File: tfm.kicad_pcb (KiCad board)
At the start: 2 copper layers, 100 x 90 mm, 93 parts, among them J1 Screw_Terminal_01x04, J2 Screw_Terminal_01x04, J3 Conn_01x03, J4 Conn_01x03, J5 Conn_01x03, J6 Conn_02x04_Counter_Clockwise, U1 LPS25HB, U10 MCP6004, U11 MCP6004, U12 ZMPT101B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

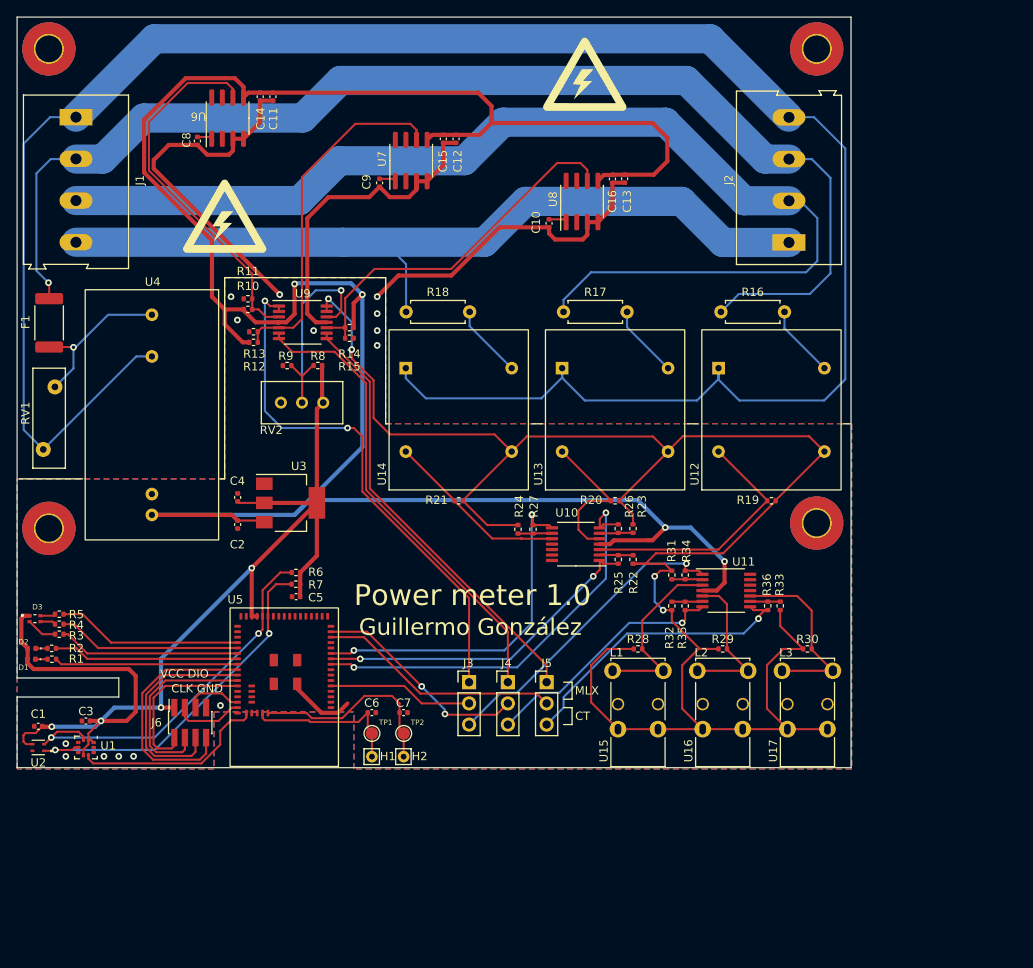
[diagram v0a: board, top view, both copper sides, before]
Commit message: Edge cuts with curves
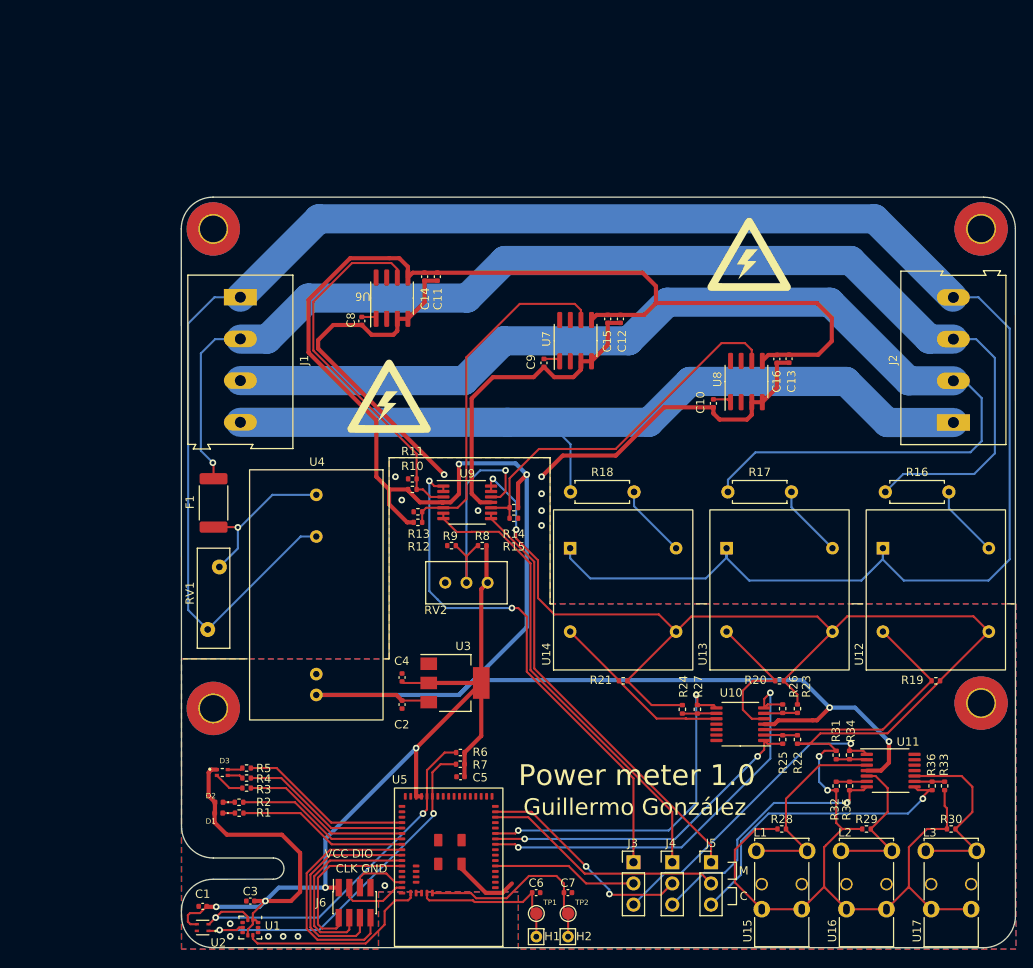
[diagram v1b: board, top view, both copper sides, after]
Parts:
- moved R16 29.2 mm to (182.9, 82.3)
- moved F1 29.2 mm to (102.3, 83.7)
- moved R8 29.2 mm to (134.5, 88.8)
- moved R9 29.2 mm to (130.8, 88.8)
- moved C1 29.2 mm to (101.0, 132.0)
- moved C10 29.2 mm to (162.2, 71.7)
- moved C11 29.2 mm to (129.1, 56.5)
- moved C12 29.2 mm to (151.1, 61.6)
- moved C14 29.2 mm to (127.6, 56.5)
- moved C15 29.2 mm to (149.6, 61.6)
- moved C16 29.2 mm to (169.8, 66.4)
- moved C2 29.2 mm to (124.9, 107.8)
- moved C3 29.2 mm to (106.7, 131.4)
- moved C4 29.2 mm to (124.9, 104.6)
- moved C8 29.2 mm to (120.1, 61.8)
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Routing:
- net /power_sensors/2V5: track 226.8 -> 221.7 mm
- net Net-(R28-Pad2): track 22.2 -> 24.8 mm
- net /power_sensors/ct3_out: track 35.0 -> 36.6 mm
- net /LED2: track 22.3 -> 20.9 mm
- net /LEDB: track 22.3 -> 20.8 mm
- net /LED1: track 22.0 -> 20.6 mm
- net /LEDG: track 22.0 -> 20.6 mm
- net /LEDR: track 21.8 -> 20.4 mm
- net /power_sensors/ct2_out: track 29.9 -> 31.3 mm
- net +3V3: track 135.1 -> 134.3 mm
- net Net-(R30-Pad2): track 22.5 -> 23.1 mm
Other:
- outline, holes or cut-outs redrawn
- board text added: "C"
- board text added: "M"
- board text removed: "CT"
- board text removed: "MLX"

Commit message: Fix jack orientation and add 3d model
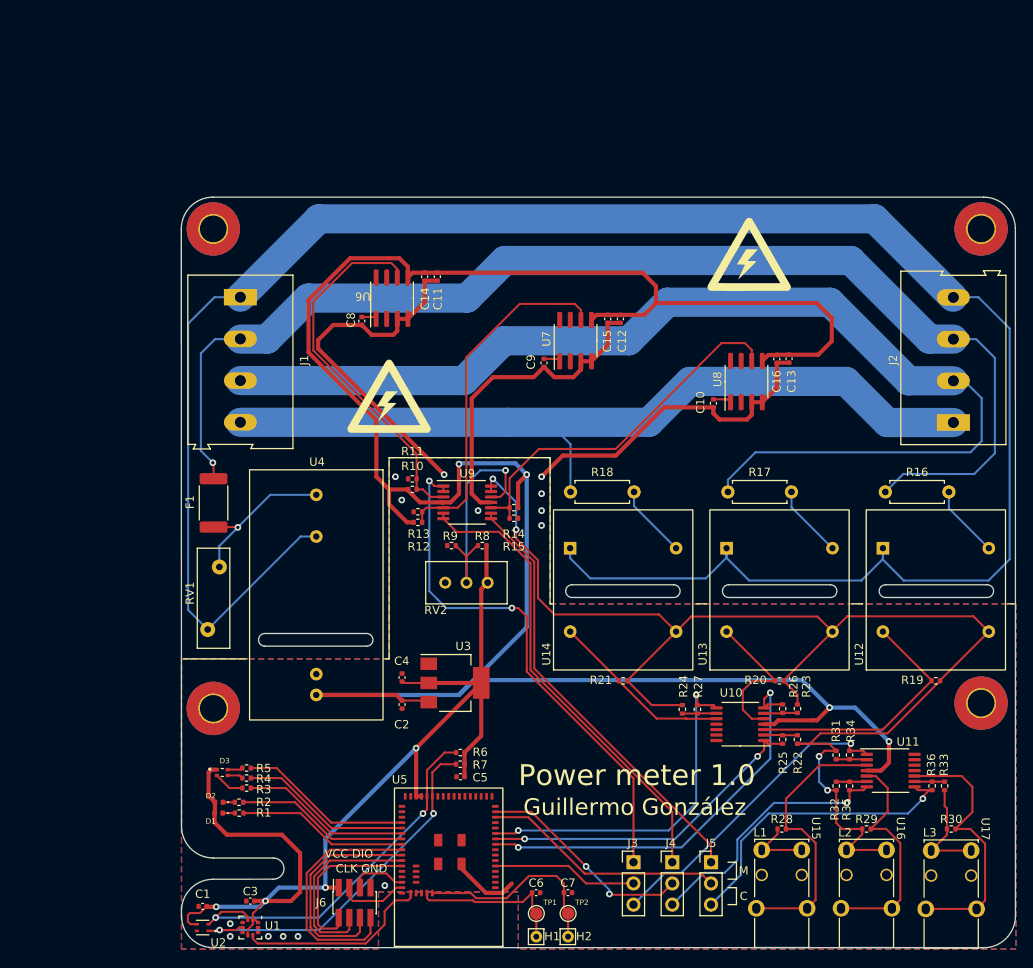
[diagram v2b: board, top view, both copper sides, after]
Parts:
- moved U15 1.11 mm to (170.4, 128.3), turned to -90 degrees
- moved U16 1.11 mm to (180.6, 128.3), turned to -90 degrees
- moved U17 1.03 mm to (190.8, 128.3), turned to -90 degrees
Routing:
- net /power_sensors/2V5: track 221.7 -> 183.7 mm
- net Net-(R30-Pad2): track 23.1 -> 32.1 mm
- net Net-(R28-Pad2): track 24.8 -> 33.7 mm
- net Net-(R29-Pad2): track 18.6 -> 27.5 mm
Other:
- outline, holes or cut-outs redrawn

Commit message: Minor changes
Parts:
- removed H1, H2: MountingHole_Pad, Connector_Pin:Pin_D0.7mm_L6.5mm_W1.8mm_FlatFork
- added J7: Conn_01x02_Female, Connector_PinHeader_2.54mm:PinHeader_1x02_P2.54mm_Vertical, F.Cu at (142.2, 135.4)
- moved TP1 1.36 mm to (142.2, 132.3)
- moved C6 1.30 mm to (142.2, 130.0), turned to 180 degrees
- moved TP2 0.56 mm to (144.8, 132.3)
- moved C7 0.34 mm to (144.8, 130.0)
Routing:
- net /power_sensors/2V5: track 183.7 -> 194.5 mm
- net /NFC1: track 19.4 -> 21.0 mm
- net GND: track 129.8 -> 130.6 mm, vias 14 -> 16
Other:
- board text added: "Mayo 2022"

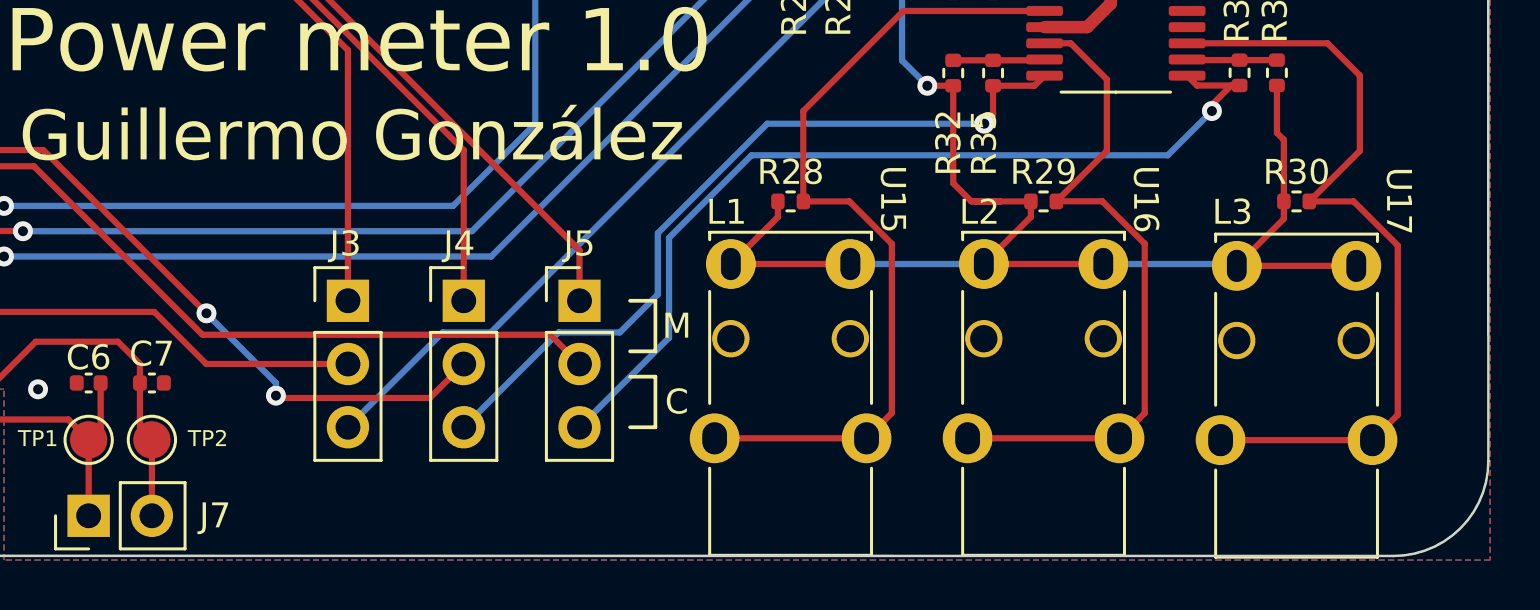
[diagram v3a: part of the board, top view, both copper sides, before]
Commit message: Fix PCB warnings
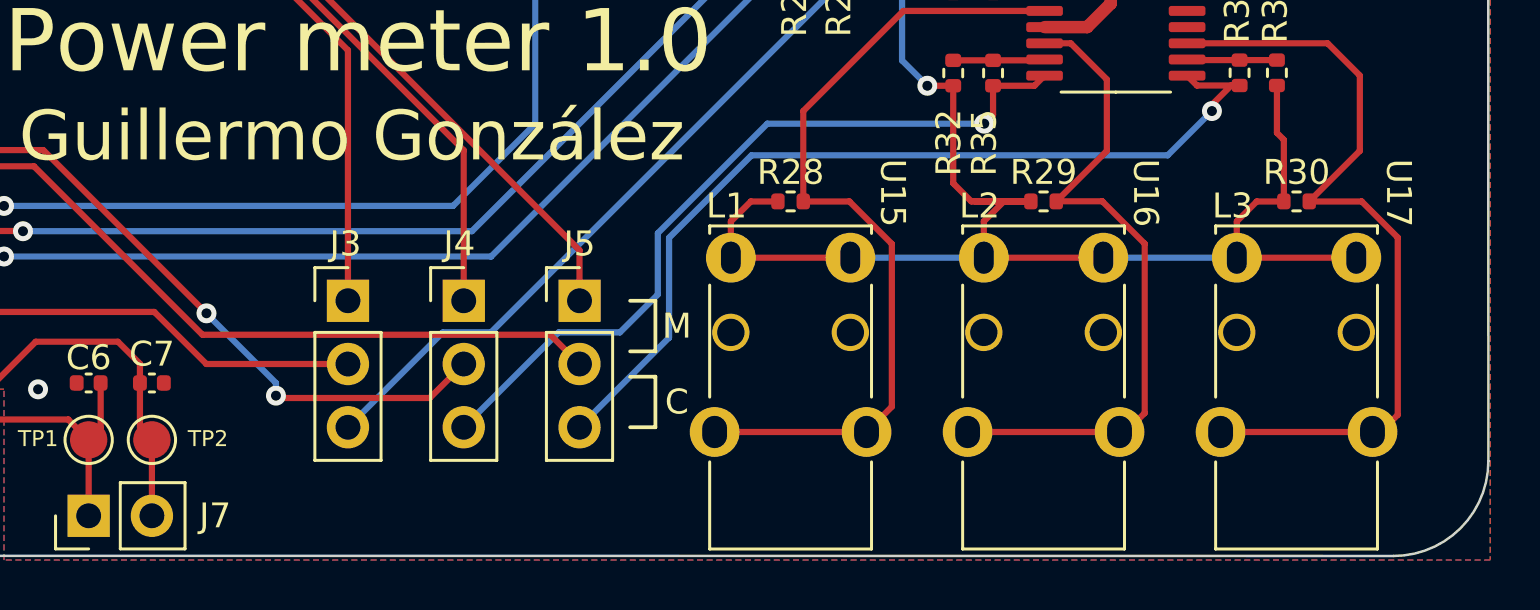
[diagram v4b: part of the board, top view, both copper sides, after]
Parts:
- moved U17 0.33 mm to (190.8, 128.0)
- moved U15 0.25 mm to (170.4, 128.0)
- moved U16 0.25 mm to (180.6, 128.0)
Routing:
- net /power_sensors/2V5: track 194.5 -> 195.5 mm

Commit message: Update 3d references and add testpoints
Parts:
- added TP3: TestPoint, TestPoint:TestPoint_Pad_D1.5mm, F.Cu at (188.5, 110.2)
- added TP4: TestPoint, TestPoint:TestPoint_Pad_D1.5mm, F.Cu at (182.6, 106.2)
- added TP5: TestPoint, TestPoint:TestPoint_Pad_D1.5mm, F.Cu at (164.1, 106.2)
- added TP6: TestPoint, TestPoint:TestPoint_Pad_D1.5mm, F.Cu at (145.8, 106.2)
- added TP7: TestPoint, TestPoint:TestPoint_Pad_D1.5mm, F.Cu at (175.5, 123.4)
- added TP8: TestPoint, TestPoint:TestPoint_Pad_D1.5mm, F.Cu at (185.9, 123.2)
- added TP9: TestPoint, TestPoint:TestPoint_Pad_D1.5mm, F.Cu at (196.1, 122.9)
- F1: footprint Fuse:Fuse_2512_6332Metric -> guille_3rdparty:Fuse_2512_6332Metric
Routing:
- net /power_sensors/2V5: track 195.5 -> 201.2 mm
- net Net-(R21-Pad2): track 21.9 -> 27.5 mm
- net Net-(R19-Pad2): track 30.8 -> 34.5 mm
- net Net-(R29-Pad2): track 27.4 -> 29.2 mm
- net Net-(R30-Pad2): track 32.2 -> 34.0 mm
- net Net-(R20-Pad2): track 18.0 -> 19.7 mm
- net Net-(R28-Pad2): track 33.3 -> 34.8 mm
